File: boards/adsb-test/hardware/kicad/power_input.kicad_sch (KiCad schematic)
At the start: 0 parts

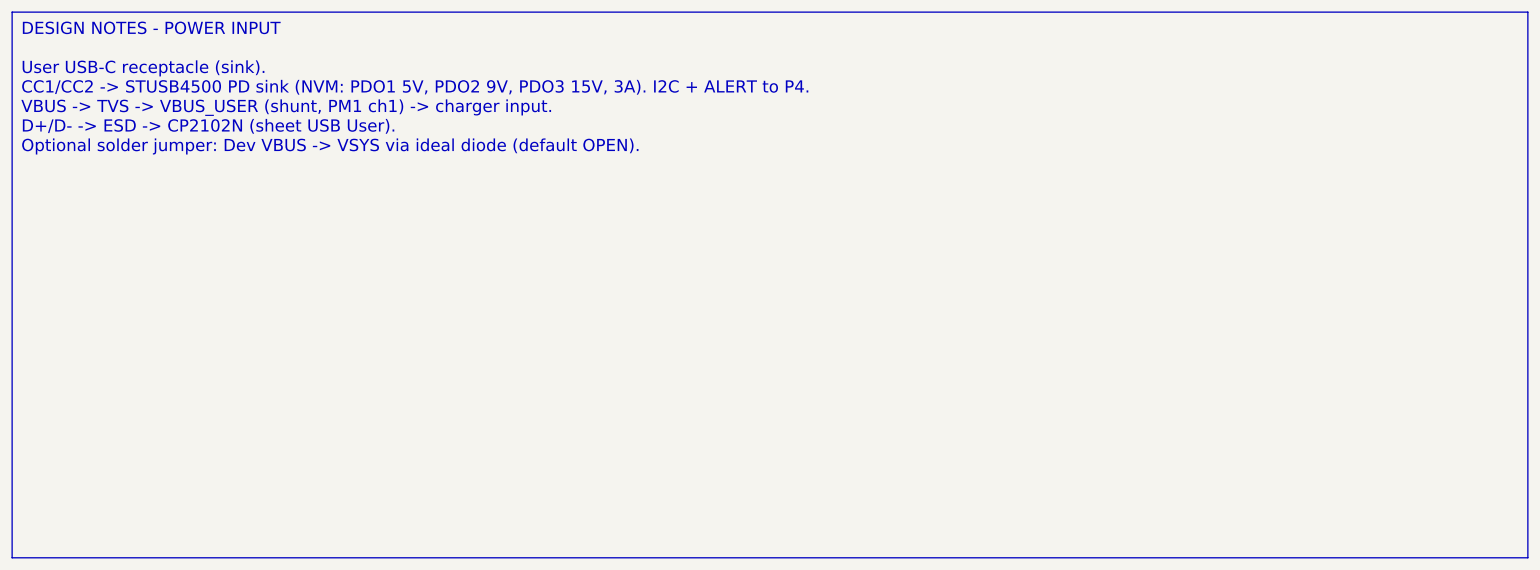
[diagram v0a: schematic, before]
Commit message: Release v0.4.0: ADSB_Test with ESP32-C5, ADSBee m1421 and LA5016 header
- C6 -> C5 co-processor; m1421 identified and integrated (symbol/footprint
  from the ADSBee 1421 carrier, GPL-3.0 attribution)
- Power budget and 2S1P battery sizing for >= 1 h; USB-A for 1-2 SDRs via hub
- Dev port: FT2232H + RP2040 debugprobe; TCA6408A expander for slow I/O
- Test Debug sheet with LA5016 header and rail test points
- Vendor documents git-ignored (public repo)

Co-Authored-By: Claude Opus 5.5 <noreply@anthropic.com>
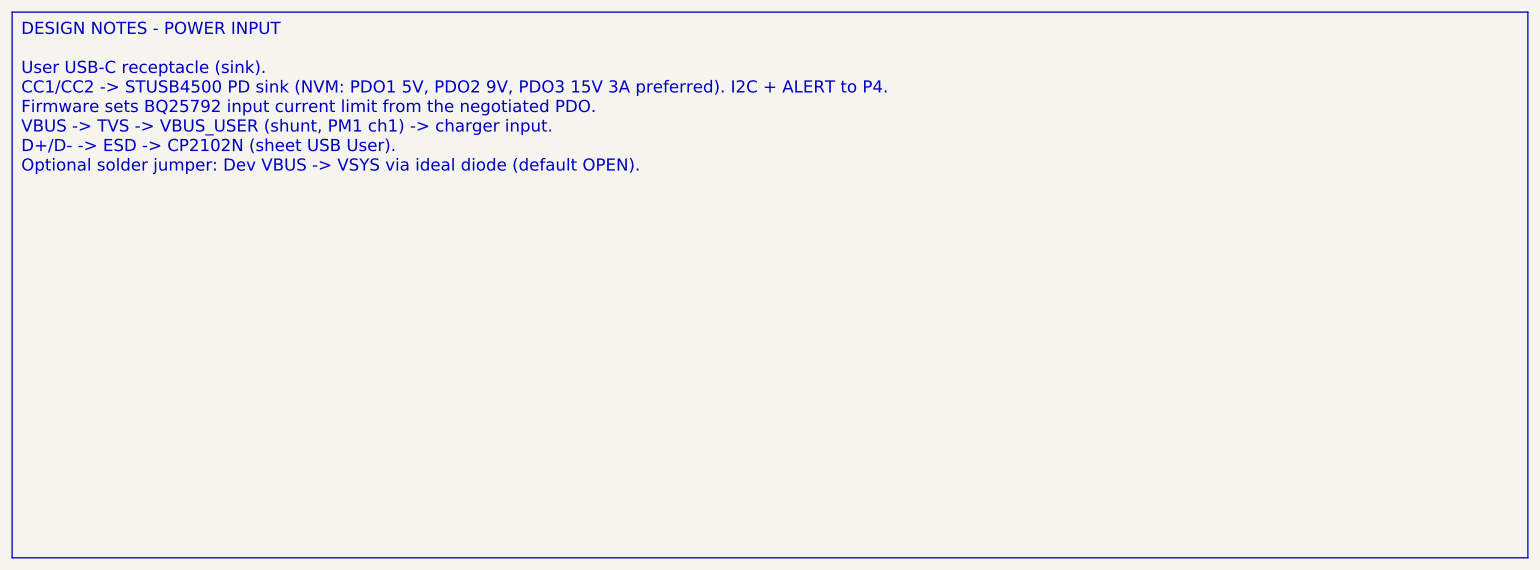
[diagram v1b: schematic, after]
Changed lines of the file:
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@@
 		(comment 1 "Requirements: boards/adsb-test/docs/requirements.md")
 	)
-	(text_box "DESIGN NOTES - POWER INPUT\n\nUser USB-C receptacle (sink).\nCC1/CC2 -> STUSB4500 PD sink (NVM: PDO1 5V, PDO2 9V, PDO3 15V, 3A). I2C + ALERT to P4.\nVBUS -> TVS -> VBUS_USER (shunt, PM1 ch1) -> charger input.\nD+/D- -> ESD -> CP2102N (sheet USB User).\nOptional solder jumper: Dev VBUS -> VSYS via ideal diode (default OPEN)."
+	(text_box "DESIGN NOTES - POWER INPUT\n\nUser USB-C receptacle (sink).\nCC1/CC2 -> STUSB4500 PD sink (NVM: PDO1 5V, PDO2 9V, PDO3 15V 3A preferred). I2C + ALERT to P4.\nFirmware sets BQ25792 input current limit from the negotiated PDO.\nVBUS -> TVS -> VBUS_USER (shunt, PM1 ch1) -> charger input.\nD+/D- -> ESD -> CP2102N (sheet USB User).\nOptional solder jumper: Dev VBUS -> VSYS via ideal diode (default OPEN)."
 		(exclude_from_sim no)
 		(at 20 20 0)
